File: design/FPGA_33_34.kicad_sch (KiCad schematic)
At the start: 22 parts

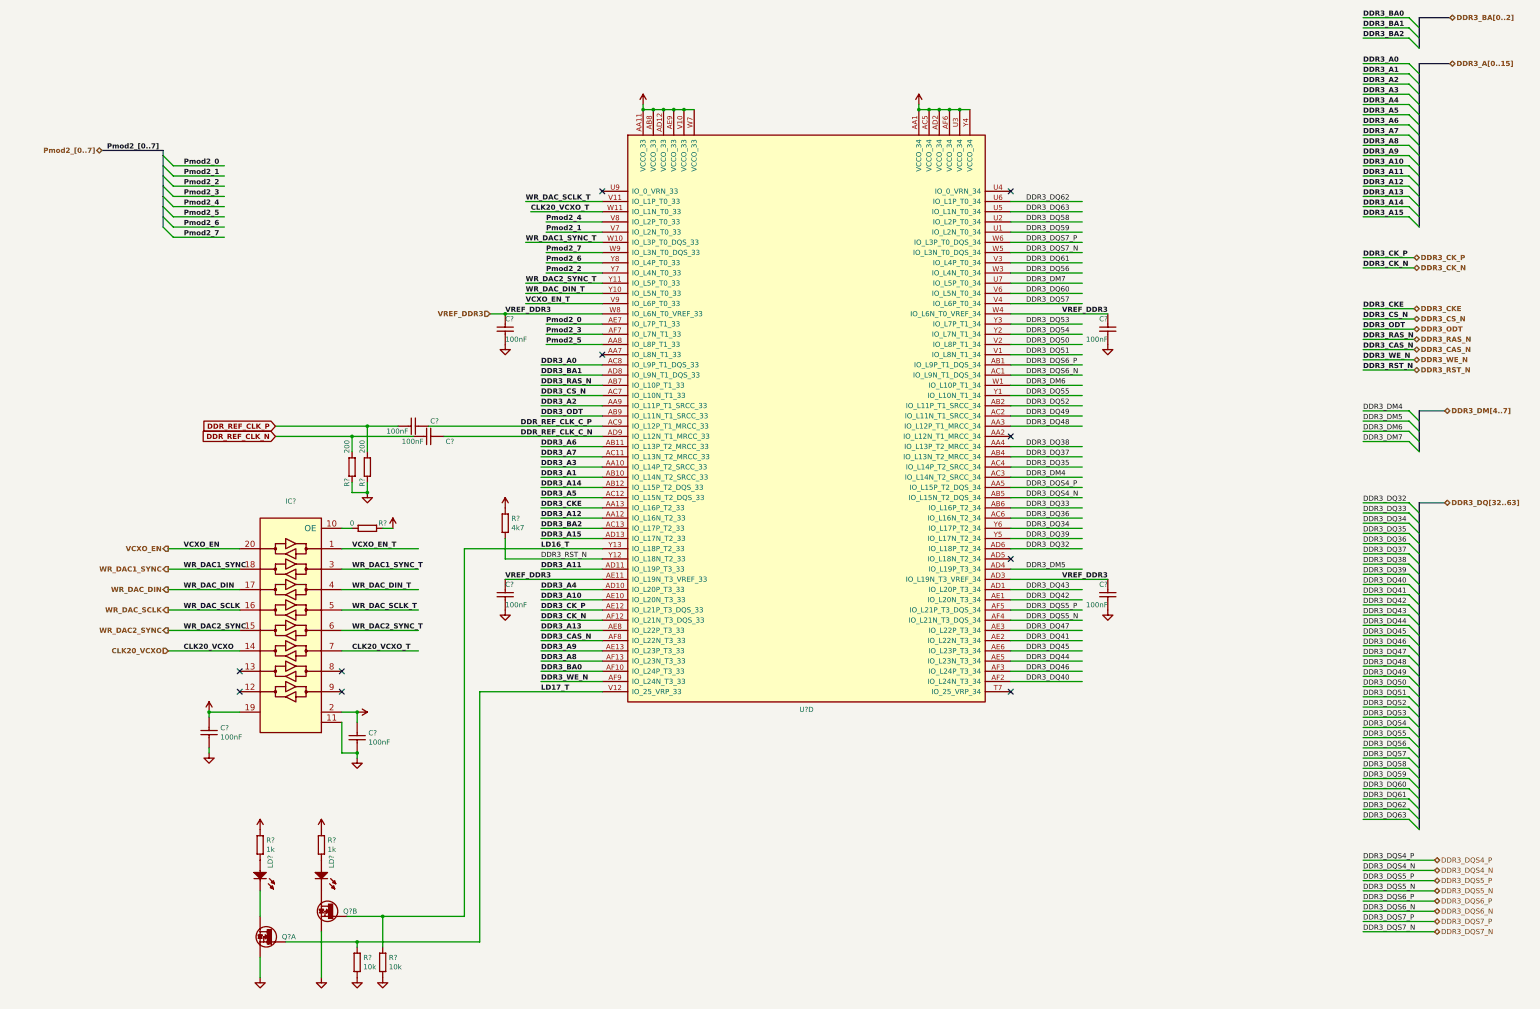
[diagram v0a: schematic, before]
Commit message: new power converter added
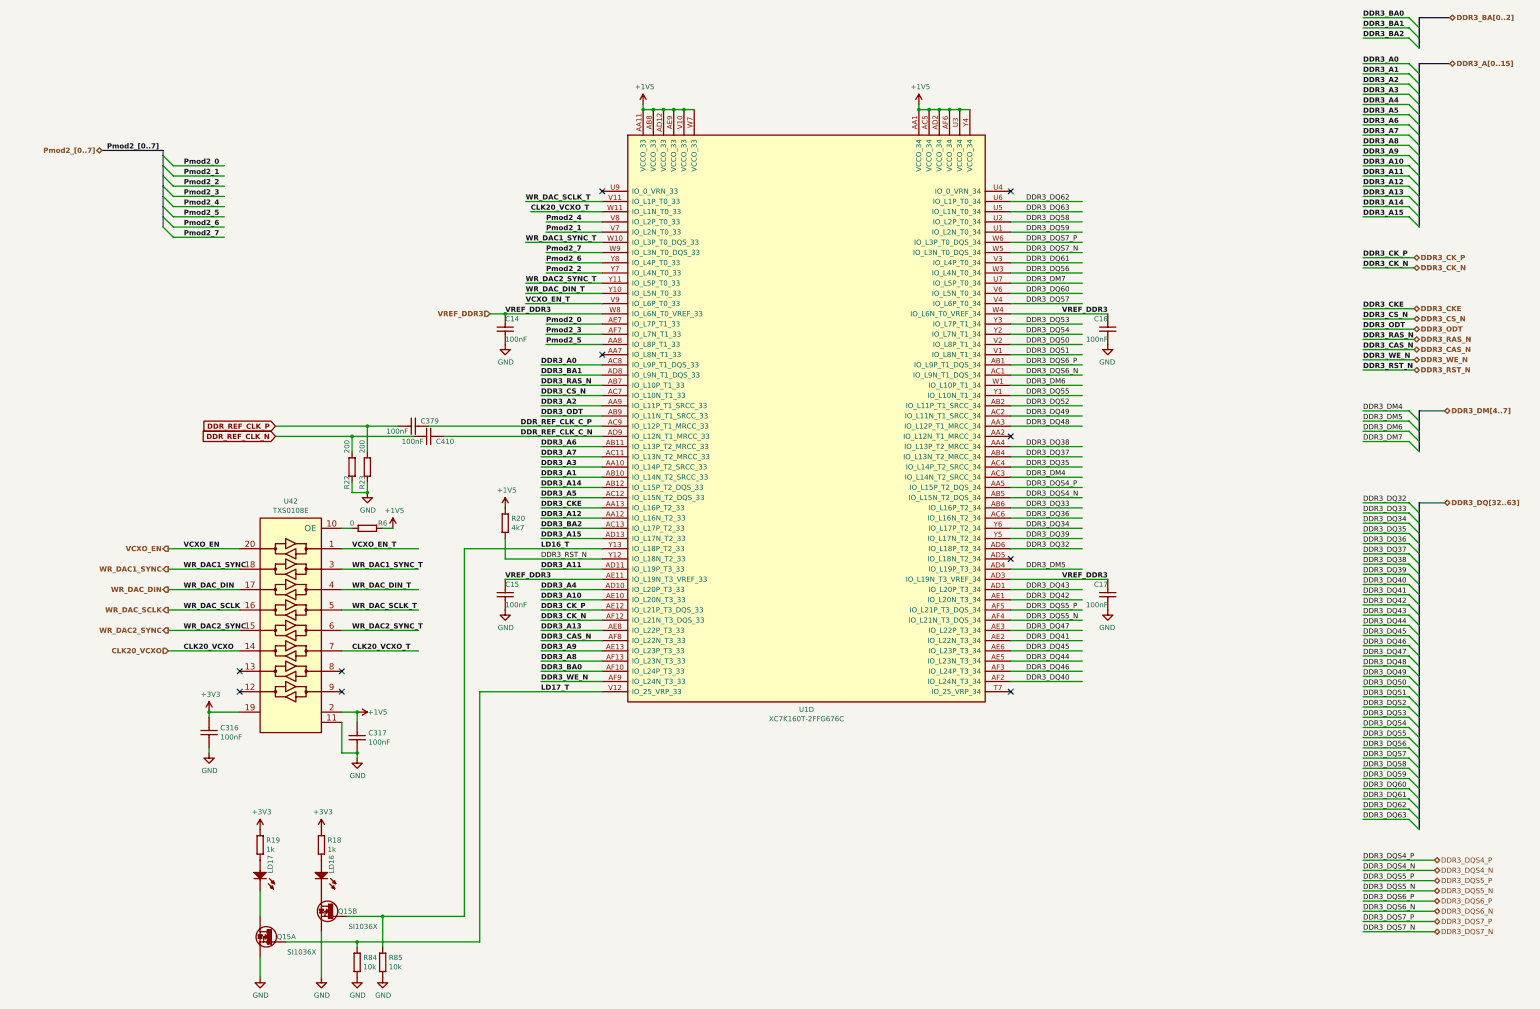
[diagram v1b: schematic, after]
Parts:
- C14, C15, C16, C17, C316, C317, C379, C410: renamed from C?; value (none) -> CC0201_100NF_6.3V_10%_X5R; footprint (none) -> CAPC0603X33N
- LD16, LD17: renamed from LD?; value (none) -> LED_KINGBRIGHT_KPH-1608CGCK; footprint (none) -> ICs And Semiconductors SMD:LED_KINGBRIGHT_KPH-1608CGCK
- Q15: renamed from Q?; value (none) -> SI1036X; footprint (none) -> ICs And Semiconductors SMD:SOTFL50P160X60-6N
- R18, R19: renamed from R?; value (none) -> R0402_1K_1%_0.0625W_100PPM; footprint (none) -> RESC1005X40N
- R20: renamed from R?; value (none) -> R0402_4K7_1%_0.0625W_100PPM; footprint (none) -> Resistors SMD:RESC1005X40N
- R22, R23: renamed from R?; value (none) -> R0201_200R_1%_0.05W_200PPM; footprint (none) -> RESC0603X28N
- R6: renamed from R?; value (none) -> R0402_0R_JUMPER; footprint (none) -> RESC1005X40N
- R84, R85: renamed from R?; value (none) -> R0402_10K_1%_0.0625W_100PPM; footprint (none) -> RESC1005X40N
- U1: renamed from U?; value (none) -> XC7K160T-2FFG676C; footprint (none) -> ICs And Semiconductors SMD_BGA:BGA676C100P26X26_2700X2700X260
- U42: renamed from IC?; value (none) -> TXS0108E; footprint (none) -> ICs And Semiconductors SMD:SOP65P640X120-20N

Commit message: connected signals to the J9 connector
connected signals to the J9 connector
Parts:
- C14, C15, C16, C17, C316, C317, C379, C410, R18, R19, R20, R22, R23, R6, R84, R85: Author CERN DEM JLC -> (none)
- LD16, LD17: Author CERN DEM JLC -> (none); Bonding No -> (none); Color Green -> (none)
- U42: Author CERN DEM MR -> (none); Bonding No -> (none)
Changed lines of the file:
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@@
       (effects (font (size 1.524 1.524)) (justify left) hide)
     )
-    (property "Author" "CERN DEM JLC" (id 35) (at -23.114 195.58 0)
+    (property "Author" "" (id 35) (at -23.114 195.58 0)
       (effects (font (size 1.524 1.524)) (justify left) hide)
     )
@@
       (effects (font (size 1.524 1.524)) (justify left) hide)
     )
-    (property "Author" "CERN DEM JLC" (id 35) (at 13.716 196.85 0)
+    (property "Author" "" (id 35) (at 13.716 196.85 0)
       (effects (font (size 1.524 1.524)) (justify left) hide)
     )
@@
       (effects (font (size 1.524 1.524)) (justify left) hide)
     )
-    (property "Author" "CERN DEM JLC" (id 36) (at 190.5 137.16 0)
+    (property "Author" "" (id 36) (at 190.5 137.16 0)
       (effects (font (size 1.524 1.524)) (justify left) hide)
     )
@@
       (effects (font (size 1.524 1.524)) (justify left) hide)
     )
-    (property "Author" "CERN DEM JLC" (id 36) (at 186.69 137.16 0)
+    (property "Author" "" (id 36) (at 186.69 137.16 0)
       (effects (font (size 1.524 1.524)) (justify left) hide)
     )
@@
       (effects (font (size 1.27 1.27)) (justify left) hide)
     )
-    (property "Author" "CERN DEM JLC" (id 35) (at 99.06 216.408 0)
+    (property "Author" "" (id 35) (at 99.06 216.408 0)
       (effects (font (size 1.27 1.27)) (justify left) hide)
     )
@@
       (effects (font (size 1.524 1.524)) (justify left) hide)
     )
-    (property "Color" "Green" (id 10) (at 65.024 234.95 0)
+    (property "Color" "" (id 10) (at 65.024 234.95 0)
       (effects (font (size 1.524 1.524)) (justify left) hide)
     )
@@
       (effects (font (size 1.524 1.524)) (justify left) hide)
     )
-    (property "Bonding" "No" (id 25) (at 28.448 234.95 0)
+    (property "Bonding" "" (id 25) (at 28.448 234.95 0)
       (effects (font (size 1.524 1.524)) (justify left) hide)
     )
@@
       (effects (font (size 1.524 1.524)) (justify left) hide)
     )
-    (property "Author" "CERN DEM JLC" (id 32) (at 5.588 234.95 0)
+    (property "Author" "" (id 32) (at 5.588 234.95 0)
       (effects (font (size 1.524 1.524)) (justify left) hide)
     )
@@
       (effects (font (size 1.524 1.524)) (justify left) hide)
     )
-    (property "Color" "Green" (id 10) (at 49.784 234.95 0)
+    (property "Color" "" (id 10) (at 49.784 234.95 0)
       (effects (font (size 1.524 1.524)) (justify left) hide)
     )
@@
       (effects (font (size 1.524 1.524)) (justify left) hide)
     )
-    (property "Bonding" "No" (id 25) (at 13.208 234.95 0)
+    (property "Bonding" "" (id 25) (at 13.208 234.95 0)
       (effects (font (size 1.524 1.524)) (justify left) hide)
     )
@@
       (effects (font (size 1.524 1.524)) (justify left) hide)
     )
-    (property "Author" "CERN DEM JLC" (id 32) (at -9.652 234.95 0)
+    (property "Author" "" (id 32) (at -9.652 234.95 0)
       (effects (font (size 1.524 1.524)) (justify left) hide)
     )
@@
       (effects (font (size 1.524 1.524)) (justify left) hide)
     )
-    (property "Author" "CERN DEM JLC" (id 35) (at 118.11 36.576 0)
+    (property "Author" "" (id 35) (at 118.11 36.576 0)
       (effects (font (size 1.524 1.524)) (justify left) hide)
     )
@@
       (effects (font (size 1.524 1.524)) (justify left) hide)
     )
-    (property "Author" "CERN DEM JLC" (id 35) (at 121.92 39.116 0)
+    (property "Author" "" (id 35) (at 121.92 39.116 0)
       (effects (font (size 1.524 1.524)) (justify left) hide)
     )
@@
       (effects (font (size 1.524 1.524)) (justify left) hide)
     )
-    (property "Author" "CERN DEM JLC" (id 36) (at 49.53 143.51 0)
+    (property "Author" "" (id 36) (at 49.53 143.51 0)
       (effects (font (size 1.524 1.524)) (justify left) hide)
     )
@@
       (effects (font (size 1.524 1.524)) (justify left) hide)
     )
-    (property "Author" "CERN DEM JLC" (id 36) (at 3.81 223.52 0)
+    (property "Author" "" (id 36) (at 3.81 223.52 0)
       (effects (font (size 1.524 1.524)) (justify left) hide)
     )
@@
       (effects (font (size 1.524 1.524)) (justify left) hide)
     )
-    (property "Author" "CERN DEM JLC" (id 36) (at -11.43 223.52 0)
+    (property "Author" "" (id 36) (at -11.43 223.52 0)
       (effects (font (size 1.524 1.524)) (justify left) hide)
     )
@@
       (effects (font (size 1.524 1.524)) (justify left) hide)
     )
-    (property "Author" "CERN DEM JLC" (id 36) (at 12.7 252.73 0)
+    (property "Author" "" (id 36) (at 12.7 252.73 0)
       (effects (font (size 1.524 1.524)) (justify left) hide)
     )
@@
       (effects (font (size 1.524 1.524)) (justify left) hide)
     )
-    (property "Author" "CERN DEM JLC" (id 36) (at 19.05 252.73 0)
+    (property "Author" "" (id 36) (at 19.05 252.73 0)
       (effects (font (size 1.524 1.524)) (justify left) hide)
     )
@@
       (effects (font (size 1.524 1.524)) (justify left) hide)
     )
-    (property "Author" "CERN DEM JLC" (id 35) (at 50.546 161.29 0)
+    (property "Author" "" (id 35) (at 50.546 161.29 0)
       (effects (font (size 1.524 1.524)) (justify left) hide)
     )
@@
       (effects (font (size 1.524 1.524)) (justify left) hide)
     )
-    (property "Author" "CERN DEM JLC" (id 35) (at 50.546 95.25 0)
+    (property "Author" "" (id 35) (at 50.546 95.25 0)
       (effects (font (size 1.524 1.524)) (justify left) hide)
     )
@@
       (effects (font (size 1.524 1.524)) (justify left) hide)
     )
-    (property "Author" "CERN DEM JLC" (id 35) (at 373.634 161.29 0)
+    (property "Author" "" (id 35) (at 373.634 161.29 0)
       (effects (font (size 1.524 1.524)) (justify left) hide)
     )
@@
       (effects (font (size 1.524 1.524)) (justify left) hide)
     )
-    (property "Author" "CERN DEM JLC" (id 35) (at 373.634 95.25 0)
+    (property "Author" "" (id 35) (at 373.634 95.25 0)
       (effects (font (size 1.524 1.524)) (justify left) hide)
     )
@@
       (effects (font (size 1.27 1.27)) (justify left) hide)
     )
-    (property "Bonding" "No" (id 24) (at 91.44 247.65 0)
+    (property "Bonding" "" (id 24) (at 91.44 247.65 0)
       (effects (font (size 1.27 1.27)) (justify left) hide)
     )
@@
       (effects (font (size 1.27 1.27)) (justify left) hide)
     )
-    (property "Author" "CERN DEM MR" (id 29) (at 91.44 257.175 0)
-      (effects (font (size 1.27 1.27)) (justify left) hide)
-    )
+    (property "Author" "" (id 29) (at 91.44 257.175 0)
+      (effects (font (size 1.27 1.27)) (justify left) hide)
+    )

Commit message: Attempt to add and improve BOM. Added new part numbers for some of the passives
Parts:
- R6: MANUFACTURER (none) -> GENERIC
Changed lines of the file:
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@@
       (effects (font (size 1.27 1.27)) (justify left) hide)
+    )
+    (property "MANUFACTURER" "GENERIC" (id 40) (at 99.06 148.59 0)
+      (effects (font (size 1.27 1.27)) hide)
     )
     (pin "1")

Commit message: Restore some consistency in schematic metadata
Still 13 problematic footprint names in LTM4673.kicad_sch:

BAD Dup: "Footprint" "CAPC1608X87N" "Capacitors SMD:CAPC1005X55N" in LTM4673-altium-import:0_Capacitor - non polarized
BAD Dup: "Footprint" "CAPC2012X135N" "CAPC1608X87N" in LTM4673-altium-import:1_Capacitor - non polarized
BAD Dup: "Footprint" "CAPC1608X87N" "Capacitors SMD:CAPC1005X55N" in LTM4673-altium-import:1_Capacitor - non polarized
BAD Dup: "Footprint" "CAPC3216X180N" "CAPC3225X270N" in LTM4673-altium-import:1_Capacitor - non polarized
BAD Dup: "Footprint" "CAPC1608X87N" "Capacitors SMD:CAPC1005X55N" in LTM4673-altium-import:0_Capacitor - non polarized
BAD Dup: "Footprint" "CAPC1608X87N" "Capacitors SMD:CAPC1005X55N" in LTM4673-altium-import:0_Capacitor - non polarized
BAD Dup: "Footprint" "CAPC3216X180N" "CAPC3225X270N" in LTM4673-altium-import:1_Capacitor - non polarized
BAD Dup: "Footprint" "CAPC2012X135N" "CAPC1608X87N" in LTM4673-altium-import:1_Capacitor - non polarized
BAD Dup: "Footprint" "CAPC3216X180N" "CAPC3225X270N" in LTM4673-altium-import:1_Capacitor - non polarized
BAD Dup: "Footprint" "CAPC1608X87N" "Capacitors SMD:CAPC1005X55N" in LTM4673-altium-import:0_Capacitor - non polarized
BAD Dup: "Footprint" "CAPC1608X87N" "Capacitors SMD:CAPC1005X55N" in LTM4673-altium-import:1_Capacitor - non polarized
BAD Dup: "Footprint" "CAPC3216X180N" "CAPC3225X270N" in LTM4673-altium-import:1_Capacitor - non polarized
BAD Dup: "Footprint" "CAPMP7343X310N" "Capacitor_Tantalum_SMD:CP_EIA-7343-30_AVX-N" in LTM4673-altium-import:3_Capacitor - polarized

But the Symbol Field editor in eeschema should be more useful now.
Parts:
- R6: MANUFACTURER GENERIC -> (none)
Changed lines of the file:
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@@
       (effects (font (size 1.27 1.27)) (justify left) hide)
-    )
-    (property "MANUFACTURER" "GENERIC" (id 40) (at 99.06 148.59 0)
-      (effects (font (size 1.27 1.27)) hide)
     )
     (pin "1")

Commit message: Parts substitutions
As researched by Michal
MPZ2012S102JTD25 -> MPZ2012S102ATD25
BC857BV-TP -> BCM857BV-7
TPS51200DRC -> TPS51200DRCR
TXS0108E -> TXS0108EPWR
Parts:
- U42: Manufacturer Part Number TXS0108E -> TXS0108EPWR
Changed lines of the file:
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@@
       (effects (font (size 1.27 1.27)) (justify left) hide)
     )
-    (property "Manufacturer Part Number" "TXS0108E" (id 15) (at 91.44 230.505 0)
+    (property "Manufacturer Part Number" "TXS0108EPWR" (id 15) (at 91.44 230.505 0)
       (effects (font (size 1.27 1.27)) (justify left) hide)
     )
